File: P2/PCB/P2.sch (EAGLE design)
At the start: 32 parts, among them CON1 Volume, CON2 Autosense, CON3 Noritake, IC1 ATMEGA48/88/168-AU, IC2 TPIC6B595DW, IC3 TPIC6B595DW, K1 G6H2-100, Q1 16MHz

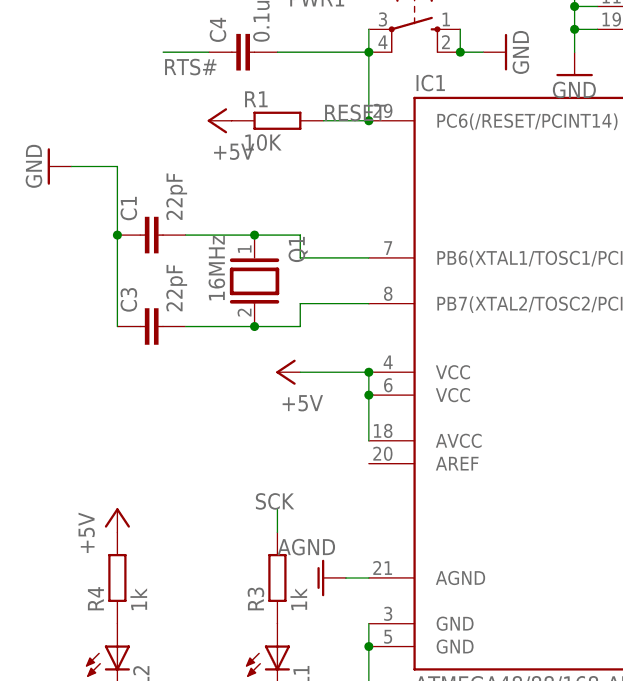
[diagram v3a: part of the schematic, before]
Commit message: Added AREF Jumper
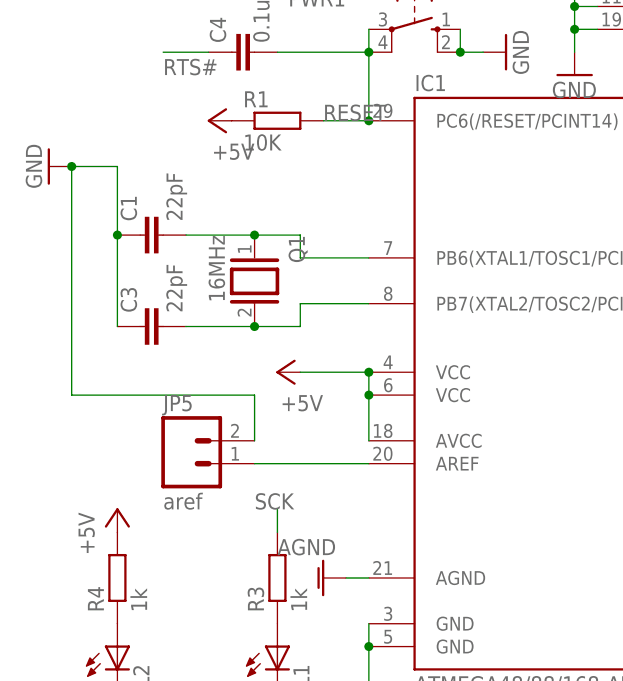
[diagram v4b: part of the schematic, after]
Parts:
- added JP5: aref, SparkFun:M02PTH
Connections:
- new net N$13: IC1.AREF, JP5.1
- net GND: now also JP5.2
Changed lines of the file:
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@@
 <part name="P+14" library="supply1" deviceset="+5V" device=""/>
 <part name="SS" library="SparkFun-Connectors" deviceset="M01" device="PTH" value="M01PTH"/>
+<part name="JP5" library="SparkFun" deviceset="M02" device="PTH" value="aref"/>
 </parts>
 <sheets>
@@
 <instance part="P+14" gate="1" x="139.7" y="60.96" rot="R180"/>
 <instance part="SS" gate="G$1" x="73.66" y="15.24"/>
+<instance part="JP5" gate="G$1" x="17.78" y="66.04"/>
 </instances>
 <busses>
@@
 <pinref part="C1" gate="G$1" pin="1"/>
 <pinref part="C3" gate="G$1" pin="1"/>
+<pinref part="JP5" gate="G$1" pin="2"/>
+<wire x1="25.4" y1="68.58" x2="25.4" y2="73.66" width="0.1524" layer="91"/>
+<wire x1="25.4" y1="73.66" x2="5.08" y2="73.66" width="0.1524" layer="91"/>
+<wire x1="5.08" y1="73.66" x2="5.08" y2="99.06" width="0.1524" layer="91"/>
+<junction x="5.08" y="99.06"/>
 </segment>
 <segment>
@@
 </segment>
 </net>
+<net name="N$13" class="0">
+<segment>
+<pinref part="JP5" gate="G$1" pin="1"/>
+<pinref part="IC1" gate="1" pin="AREF"/>
+<wire x1="25.4" y1="66.04" x2="38.1" y2="66.04" width="0.1524" layer="91"/>
+</segment>
+</net>

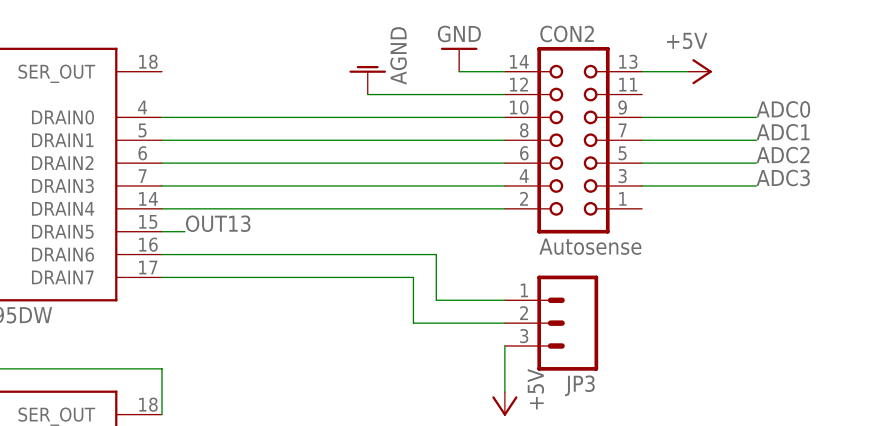
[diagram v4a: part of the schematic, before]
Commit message: P2 PCB update for peakdetect.
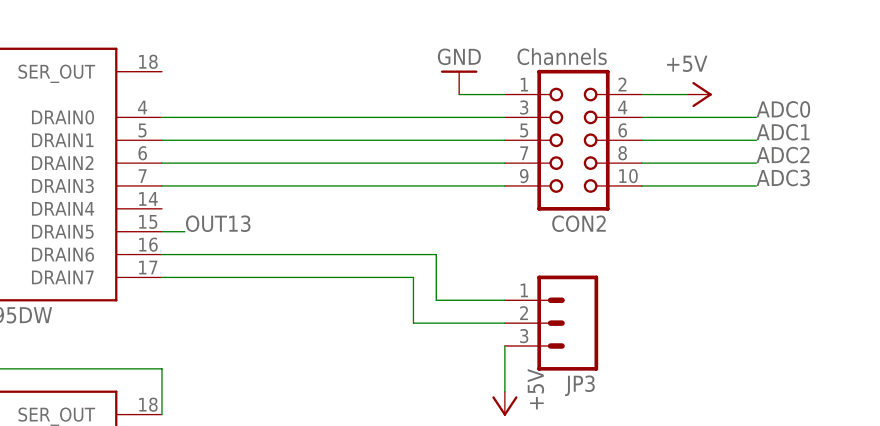
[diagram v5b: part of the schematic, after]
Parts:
- CON2: value Autosense -> Channels; device con-harting-lars:CON14L -> con-harting-lars:CON10L
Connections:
- removed net OUT12: CON2.2, IC2.DRAIN4
- net +5V: now also CON2.2; no longer CON2.13
- net ADC0: now also CON2.4; no longer CON2.9
- net ADC1: now also CON2.6; no longer CON2.7
- net ADC2: now also CON2.8; no longer CON2.5
- net ADC3: now also CON2.10; no longer CON2.3
- net AGND: no longer CON2.12
- net GND: now also CON2.1; no longer CON2.14
- net OUT10: now also CON2.7; no longer CON2.6
- net OUT11: now also CON2.9; no longer CON2.4
- net OUT8: now also CON2.3; no longer CON2.10
- net OUT9: now also CON2.5; no longer CON2.8
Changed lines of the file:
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@@
 <?xml version="1.0" encoding="utf-8"?>
 <!DOCTYPE eagle SYSTEM "eagle.dtd">
-<eagle version="6.4">
+<eagle version="8.6.1">
 <drawing>
 <settings>
 <setting alwaysvectorfont="no"/>
+<setting keepoldvectorfont="yes"/>
 <setting verticaltext="up"/>
 </settings>
@@
 <part name="P+1" library="supply1" deviceset="+5V" device=""/>
 <part name="P+4" library="supply1" deviceset="+5V" device=""/>
-<part name="CON2" library="con-harting-lars" deviceset="CON14L" device="" value="Autosense"/>
 <part name="P+10" library="supply1" deviceset="+5V" device=""/>
 <part name="GND14" library="supply1" deviceset="GND" device=""/>
-<part name="AGND1" library="supply1" deviceset="AGND" device=""/>
 <part name="AGND2" library="supply1" deviceset="AGND" device=""/>
 <part name="K1" library="relay" deviceset="G6H2-100" device=""/>
@@
 <part name="SS" library="SparkFun-Connectors" deviceset="M01" device="PTH" value="M01PTH"/>
 <part name="JP5" library="SparkFun" deviceset="M02" device="PTH" value="aref"/>
+<part name="CON2" library="con-harting-lars" deviceset="CON10L" device="" value="Channels"/>
 </parts>
 <sheets>
@@
 <instance part="P+1" gate="1" x="50.8" y="160.02" rot="R90"/>
 <instance part="P+4" gate="1" x="50.8" y="121.92" rot="R90"/>
-<instance part="CON2" gate="G$1" x="142.24" y="167.64"/>
-<instance part="P+10" gate="1" x="157.48" y="175.26" rot="R270"/>
-<instance part="GND14" gate="1" x="129.54" y="177.8" rot="R180"/>
-<instance part="AGND1" gate="VR1" x="119.38" y="175.26" rot="R180"/>
+<instance part="P+10" gate="1" x="157.48" y="172.72" rot="R270"/>
+<instance part="GND14" gate="1" x="129.54" y="175.26" rot="R180"/>
 <instance part="AGND2" gate="VR1" x="33.02" y="53.34" rot="R270"/>
 <instance part="K1" gate="1" x="162.56" y="96.52"/>
@@
 <instance part="SS" gate="G$1" x="73.66" y="15.24"/>
 <instance part="JP5" gate="G$1" x="17.78" y="66.04"/>
+<instance part="CON2" gate="G$1" x="142.24" y="167.64" rot="R180"/>
 </instances>
 <busses>
@@
 </segment>
 <segment>
-<pinref part="GND14" gate="1" pin="GND"/>
-<pinref part="CON2" gate="G$1" pin="14"/>
-<wire x1="129.54" y1="175.26" x2="134.62" y2="175.26" width="0.1524" layer="91"/>
-</segment>
-<segment>
 <pinref part="I2C2" gate="G$1" pin="2"/>
 <pinref part="GND15" gate="1" pin="GND"/>
@@
 <pinref part="GND3" gate="1" pin="GND"/>
 <wire x1="111.76" y1="53.34" x2="111.76" y2="43.18" width="0.1524" layer="91"/>
+</segment>
+<segment>
+<pinref part="GND14" gate="1" pin="GND"/>
+<pinref part="CON2" gate="G$1" pin="1"/>
+<wire x1="129.54" y1="172.72" x2="134.62" y2="172.72" width="0.1524" layer="91"/>
 </segment>
 </net>
@@
 </segment>
 <segment>
-<pinref part="CON2" gate="G$1" pin="13"/>
-<pinref part="P+10" gate="1" pin="+5V"/>
-<wire x1="149.86" y1="175.26" x2="154.94" y2="175.26" width="0.1524" layer="91"/>
-</segment>
-<segment>
 <pinref part="K1" gate="1" pin="2"/>
 <pinref part="P+11" gate="1" pin="+5V"/>
@@
 <pinref part="P+14" gate="1" pin="+5V"/>
 <wire x1="139.7" y1="71.12" x2="139.7" y2="63.5" width="0.1524" layer="91"/>
+</segment>
+<segment>
+<pinref part="CON2" gate="G$1" pin="2"/>
+<pinref part="P+10" gate="1" pin="+5V"/>
+<wire x1="149.86" y1="172.72" x2="154.94" y2="172.72" width="0.1524" layer="91"/>
 </segment>
 </net>
@@
 <net name="AGND" class="0">
 <segment>
-<pinref part="AGND1" gate="VR1" pin="AGND"/>
-<pinref part="CON2" gate="G$1" pin="12"/>
-<wire x1="119.38" y1="172.72" x2="134.62" y2="172.72" width="0.1524" layer="91"/>
-</segment>
-<segment>
 <pinref part="IC1" gate="1" pin="AGND"/>
 <wire x1="38.1" y1="53.34" x2="35.56" y2="53.34" width="0.1524" layer="91"/>
@@
 <segment>
 <pinref part="IC2" gate="G$1" pin="DRAIN0"/>
-<pinref part="CON2" gate="G$1" pin="10"/>
 <wire x1="96.52" y1="170.18" x2="134.62" y2="170.18" width="0.1524" layer="91"/>
+<pinref part="CON2" gate="G$1" pin="3"/>
 </segment>
 </net>
@@
 <segment>
 <pinref part="IC2" gate="G$1" pin="DRAIN1"/>
-<pinref part="CON2" gate="G$1" pin="8"/>
 <wire x1="96.52" y1="167.64" x2="134.62" y2="167.64" width="0.1524" layer="91"/>
+<pinref part="CON2" gate="G$1" pin="5"/>
 </segment>
 </net>
@@
 <segment>
 <pinref part="IC2" gate="G$1" pin="DRAIN2"/>
-<pinref part="CON2" gate="G$1" pin="6"/>
 <wire x1="96.52" y1="165.1" x2="134.62" y2="165.1" width="0.1524" layer="91"/>
+<pinref part="CON2" gate="G$1" pin="7"/>
 </segment>
 </net>
@@
 <segment>
 <pinref part="IC2" gate="G$1" pin="DRAIN3"/>
-<pinref part="CON2" gate="G$1" pin="4"/>
 <wire x1="96.52" y1="162.56" x2="134.62" y2="162.56" width="0.1524" layer="91"/>
-</segment>
-</net>
-<net name="OUT12" class="0">
-<segment>
-<pinref part="IC2" gate="G$1" pin="DRAIN4"/>
-<pinref part="CON2" gate="G$1" pin="2"/>
-<wire x1="96.52" y1="160.02" x2="134.62" y2="160.02" width="0.1524" layer="91"/>
+<pinref part="CON2" gate="G$1" pin="9"/>
 </segment>
 </net>
@@
 </segment>
 <segment>
-<pinref part="CON2" gate="G$1" pin="9"/>
 <wire x1="149.86" y1="170.18" x2="162.56" y2="170.18" width="0.1524" layer="91"/>
 <label x="162.56" y="170.18" size="1.778" layer="95"/>
+<pinref part="CON2" gate="G$1" pin="4"/>
 </segment>
 </net>
@@
 </segment>
 <segment>
-<pinref part="CON2" gate="G$1" pin="7"/>
 <wire x1="149.86" y1="167.64" x2="162.56" y2="167.64" width="0.1524" layer="91"/>
 <label x="162.56" y="167.64" size="1.778" layer="95"/>
+<pinref part="CON2" gate="G$1" pin="6"/>
 </segment>
 </net>
@@
 </segment>
 <segment>
-<pinref part="CON2" gate="G$1" pin="5"/>
 <wire x1="149.86" y1="165.1" x2="162.56" y2="165.1" width="0.1524" layer="91"/>
 <label x="162.56" y="165.1" size="1.778" layer="95"/>
+<pinref part="CON2" gate="G$1" pin="8"/>
 </segment>
 </net>
@@
 </segment>
 <segment>
-<pinref part="CON2" gate="G$1" pin="3"/>
 <wire x1="149.86" y1="162.56" x2="162.56" y2="162.56" width="0.1524" layer="91"/>
 <label x="162.56" y="162.56" size="1.778" layer="95"/>
-</segment>
-</net>
+<pinref part="CON2" gate="G$1" pin="10"/>
+</segment>
+</net>

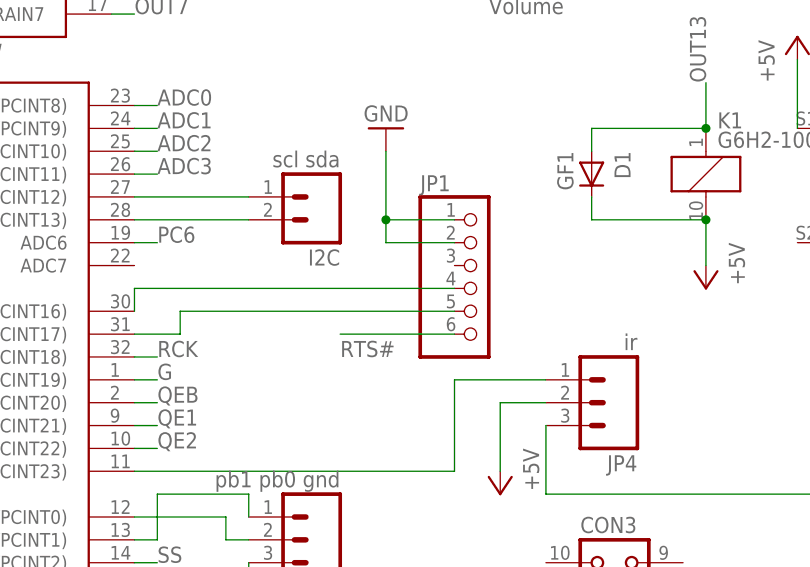
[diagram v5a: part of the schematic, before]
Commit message: Connect pin 3 of the serial connector to power. Doh.
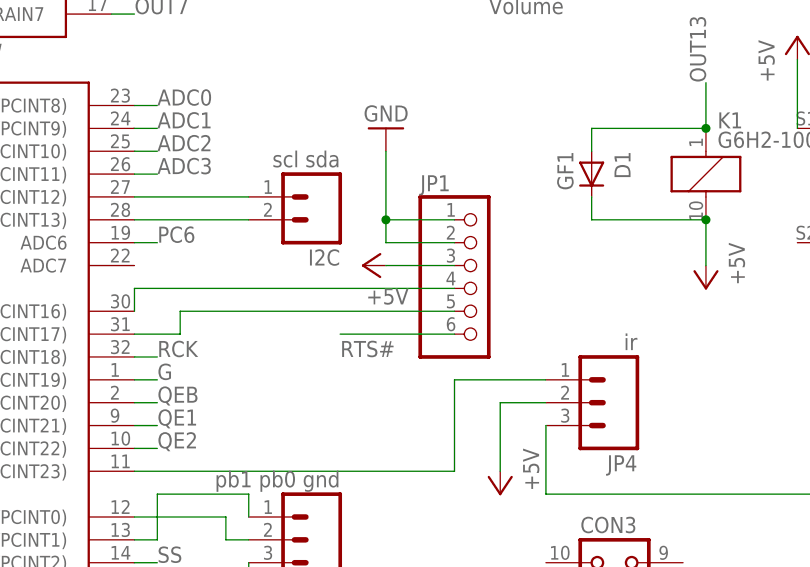
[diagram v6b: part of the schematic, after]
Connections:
- net +5V: now also JP1.3
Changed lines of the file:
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@@
 <?xml version="1.0" encoding="utf-8"?>
 <!DOCTYPE eagle SYSTEM "eagle.dtd">
-<eagle version="8.6.1">
+<eagle version="8.7.1">
 <drawing>
 <settings>
@@
 <part name="JP5" library="SparkFun" deviceset="M02" device="PTH" value="aref"/>
 <part name="CON2" library="con-harting-lars" deviceset="CON10L" device="" value="Channels"/>
+<part name="P+15" library="supply1" deviceset="+5V" device=""/>
 </parts>
 <sheets>
@@
 <instance part="JP5" gate="G$1" x="17.78" y="66.04"/>
 <instance part="CON2" gate="G$1" x="142.24" y="167.64" rot="R180"/>
+<instance part="P+15" gate="1" x="124.46" y="86.36" rot="R90"/>
 </instances>
 <busses>
@@
 <wire x1="149.86" y1="172.72" x2="154.94" y2="172.72" width="0.1524" layer="91"/>
 </segment>
+<segment>
+<pinref part="P+15" gate="1" pin="+5V"/>
+<pinref part="JP1" gate="A" pin="3"/>
+<wire x1="127" y1="86.36" x2="134.62" y2="86.36" width="0.1524" layer="91"/>
+</segment>
 </net>

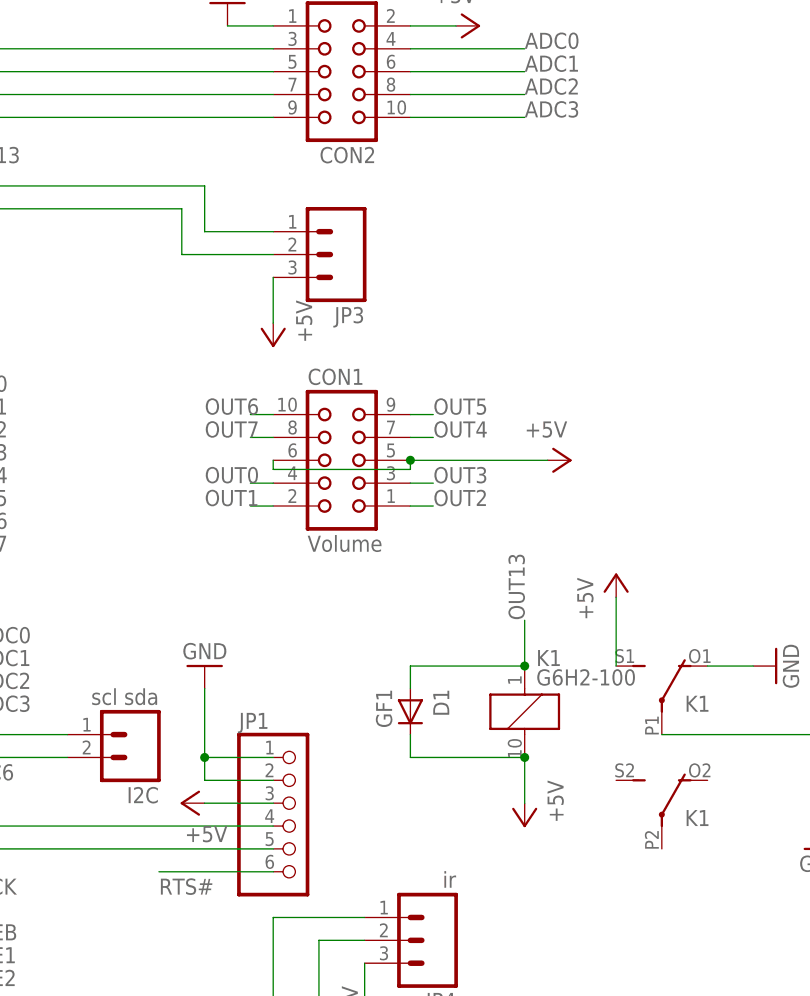
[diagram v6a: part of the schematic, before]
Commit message: Working version with heavily patched PCB
- ADC6 does not work as /SS for Noritake, use B0.
- Relay connected wrong (internal diode!)
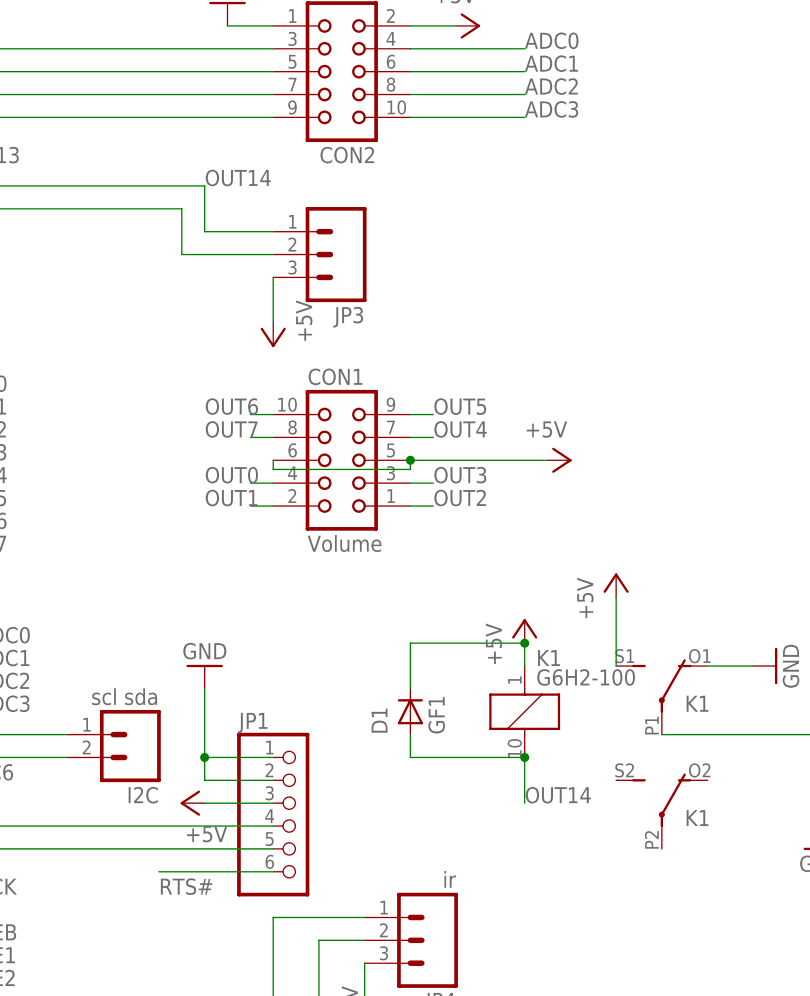
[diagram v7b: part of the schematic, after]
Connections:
- removed net N$11: IC2.DRAIN6, JP3.1
- new net OUT14: D1.A, IC2.DRAIN6, JP3.1, K11.2
- net +5V: now also K11.1; no longer K11.2
- net OUT13: no longer D1.A, K11.1
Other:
- moved on the sheet: D1
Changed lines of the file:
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@@
 <instance part="K1" gate="2" x="177.8" y="96.52"/>
 <instance part="K1" gate="3" x="177.8" y="83.82"/>
-<instance part="P+11" gate="1" x="162.56" y="83.82" rot="R180"/>
-<instance part="D1" gate="D" x="149.86" y="96.52" rot="R270"/>
+<instance part="P+11" gate="1" x="162.56" y="106.68"/>
+<instance part="D1" gate="D" x="149.86" y="96.52" rot="R90"/>
 <instance part="I2C2" gate="G$1" x="203.2" y="93.98" rot="R180"/>
 <instance part="P+12" gate="1" x="172.72" y="111.76"/>
@@
 </segment>
 <segment>
-<pinref part="K1" gate="1" pin="2"/>
-<pinref part="P+11" gate="1" pin="+5V"/>
-<wire x1="162.56" y1="91.44" x2="162.56" y2="86.36" width="0.1524" layer="91"/>
-<pinref part="D1" gate="D" pin="C"/>
-<wire x1="149.86" y1="93.98" x2="149.86" y2="91.44" width="0.1524" layer="91"/>
-<wire x1="149.86" y1="91.44" x2="162.56" y2="91.44" width="0.1524" layer="91"/>
-<junction x="162.56" y="91.44"/>
-</segment>
-<segment>
 <pinref part="P+12" gate="1" pin="+5V"/>
 <pinref part="K1" gate="2" pin="S"/>
@@
 <pinref part="JP1" gate="A" pin="3"/>
 <wire x1="127" y1="86.36" x2="134.62" y2="86.36" width="0.1524" layer="91"/>
+</segment>
+<segment>
+<pinref part="K1" gate="1" pin="1"/>
+<pinref part="P+11" gate="1" pin="+5V"/>
+<wire x1="162.56" y1="101.6" x2="162.56" y2="104.14" width="0.1524" layer="91"/>
+<pinref part="D1" gate="D" pin="C"/>
+<wire x1="149.86" y1="99.06" x2="149.86" y2="104.14" width="0.1524" layer="91"/>
+<wire x1="149.86" y1="104.14" x2="162.56" y2="104.14" width="0.1524" layer="91"/>
+<junction x="162.56" y="104.14"/>
 </segment>
 </net>
@@
 <label x="99.06" y="157.48" size="1.778" layer="95"/>
 </segment>
-<segment>
-<pinref part="K1" gate="1" pin="1"/>
-<wire x1="162.56" y1="101.6" x2="162.56" y2="106.68" width="0.1524" layer="91"/>
-<label x="162.56" y="106.68" size="1.778" layer="95" rot="R90"/>
-<pinref part="D1" gate="D" pin="A"/>
-<wire x1="149.86" y1="99.06" x2="149.86" y2="101.6" width="0.1524" layer="91"/>
-<wire x1="149.86" y1="101.6" x2="162.56" y2="101.6" width="0.1524" layer="91"/>
-<junction x="162.56" y="101.6"/>
-</segment>
 </net>
 <net name="N$5" class="0">
@@
 </segment>
 </net>
-<net name="N$11" class="0">
+<net name="OUT14" class="0">
 <segment>
 <pinref part="IC2" gate="G$1" pin="DRAIN6"/>
@@
 <pinref part="JP3" gate="G$1" pin="1"/>
 <wire x1="127" y1="149.86" x2="134.62" y2="149.86" width="0.1524" layer="91"/>
-</segment>
-</net>
+<label x="127" y="154.94" size="1.778" layer="95"/>
+</segment>
+<segment>
+<pinref part="D1" gate="D" pin="A"/>
+<wire x1="149.86" y1="93.98" x2="149.86" y2="91.44" width="0.1524" layer="91"/>
+<pinref part="K1" gate="1" pin="2"/>
+<wire x1="149.86" y1="91.44" x2="162.56" y2="91.44" width="0.1524" layer="91"/>
+<wire x1="162.56" y1="91.44" x2="162.56" y2="86.36" width="0.1524" layer="91"/>
+<junction x="162.56" y="91.44"/>
+<label x="162.56" y="86.36" size="1.778" layer="95"/>
+</segment>
+</net>
